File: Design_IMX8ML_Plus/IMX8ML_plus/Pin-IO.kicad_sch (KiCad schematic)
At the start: 3 parts, among them J1 DF40C-100DP-0.4V_51_, J2 DF40C-100DP-0.4V_51_, J3 DF40C-100DP-0.4V_51_

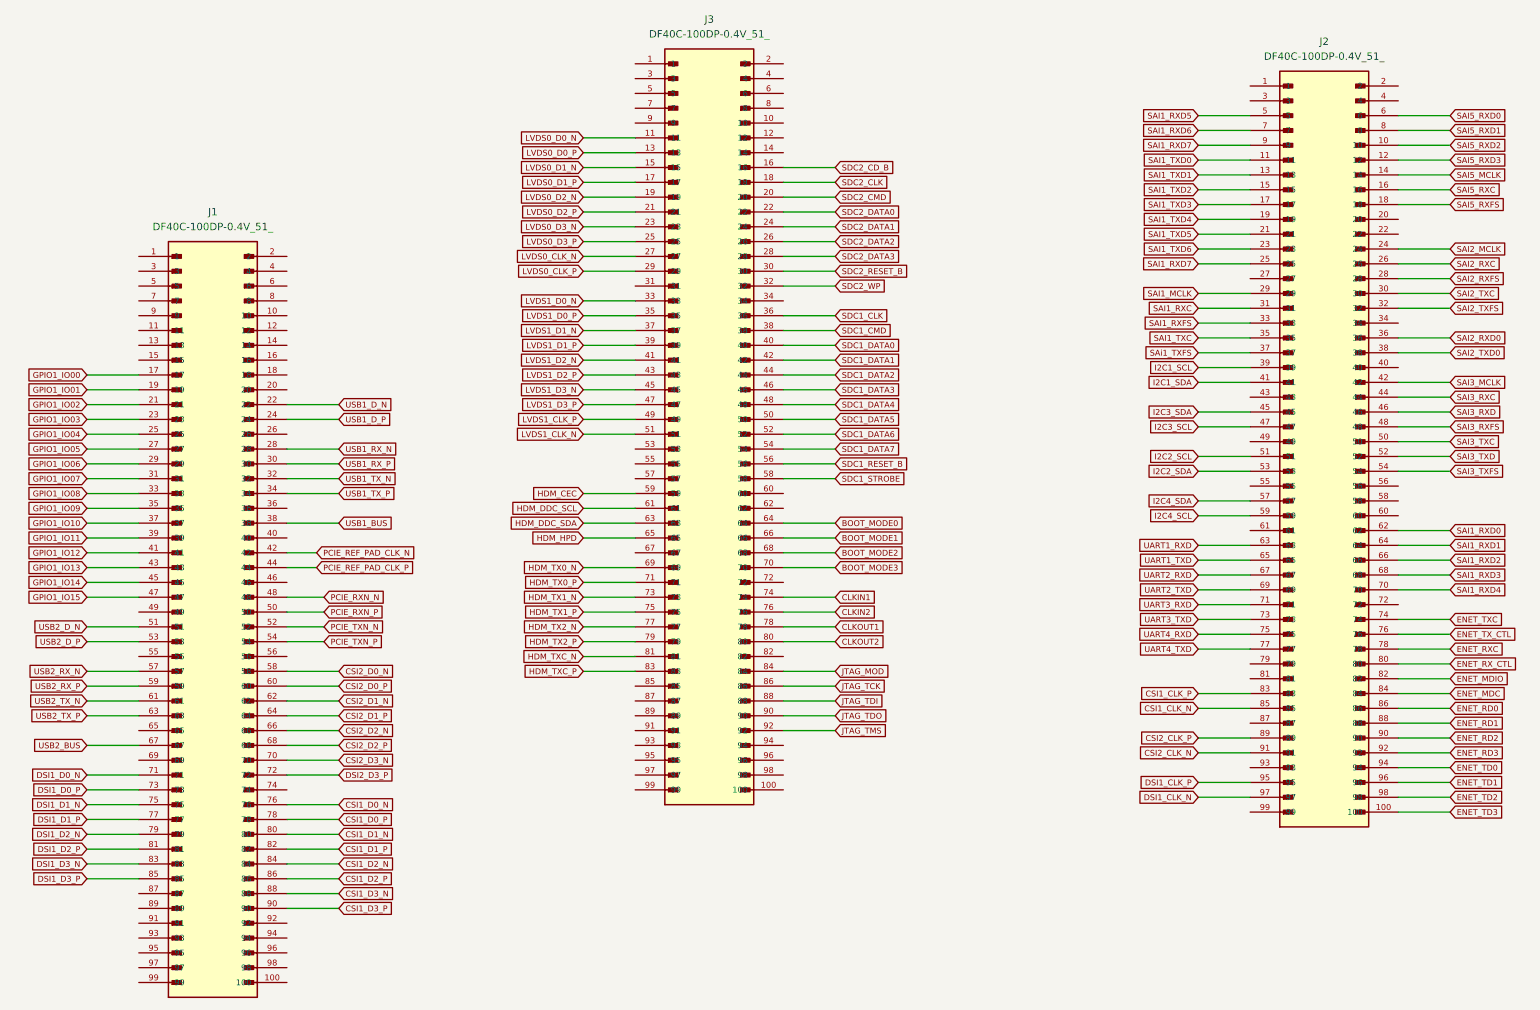
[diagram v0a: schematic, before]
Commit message: Update schematic and add ethernet interface ksz9131rn
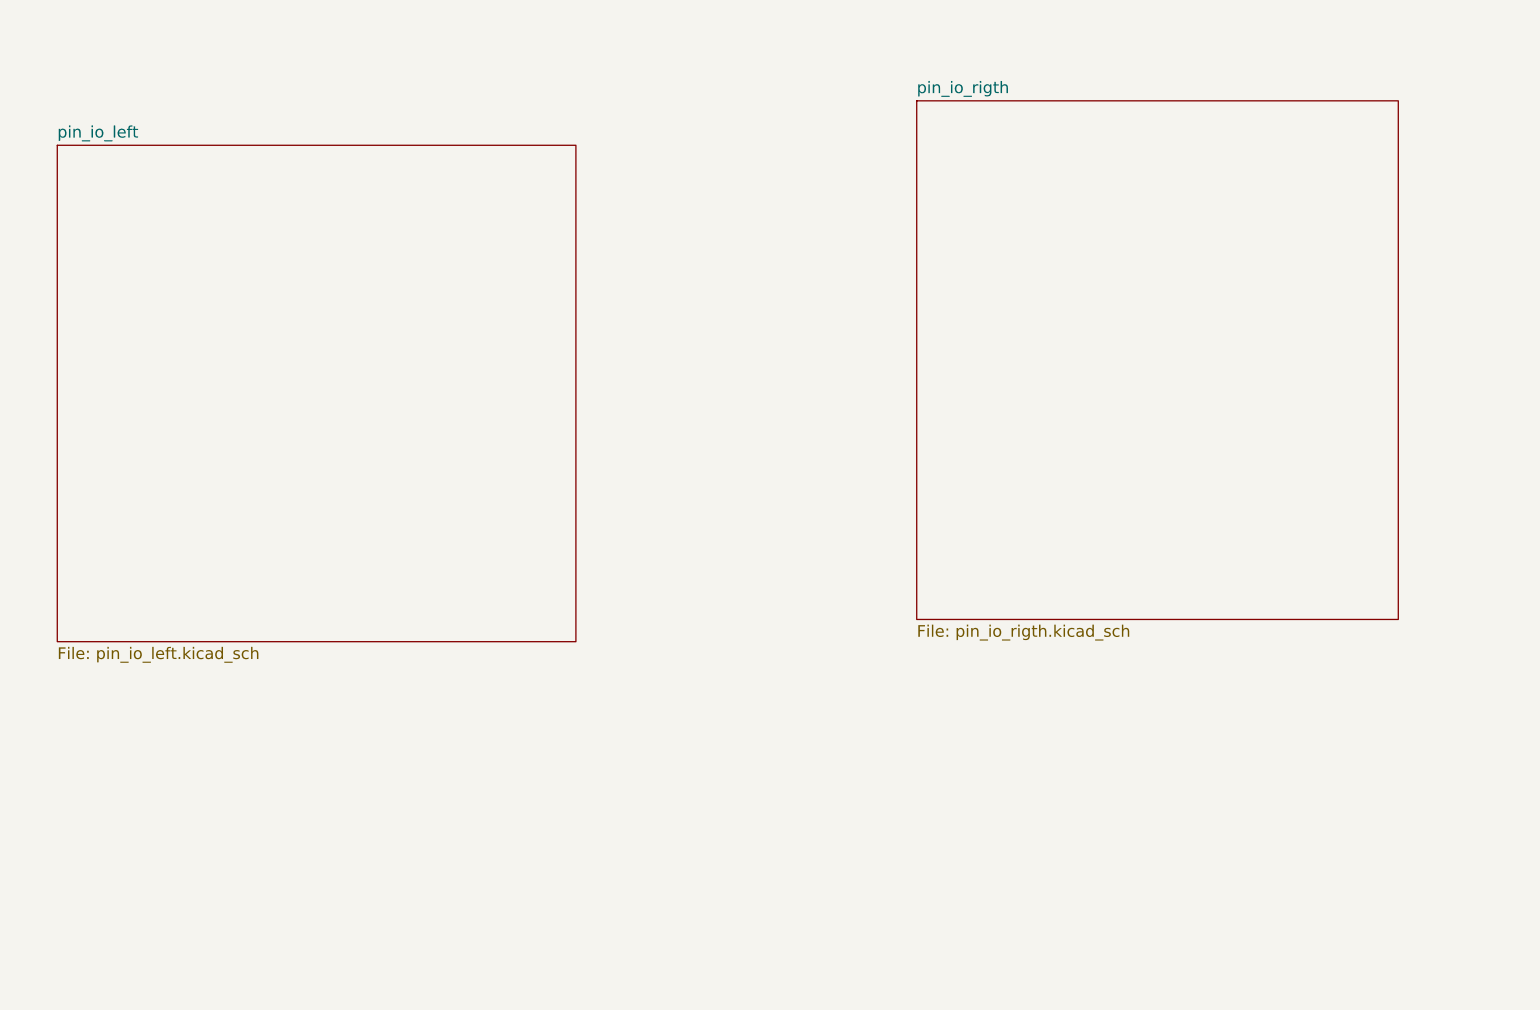
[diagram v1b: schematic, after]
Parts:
- removed J1, J2, J3: DF40C-100DP-0.4V_51_, _W_SBC:HIROSE_DF40C-100DS-0.4V_51_, symbol CONN_DF40C-100DS-0_4V51_HIR:DF40C-100DP-0.4V_51_
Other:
- added sheet pin_io_left (pin_io_left.kicad_sch)
- added sheet pin_io_rigth (pin_io_rigth.kicad_sch)

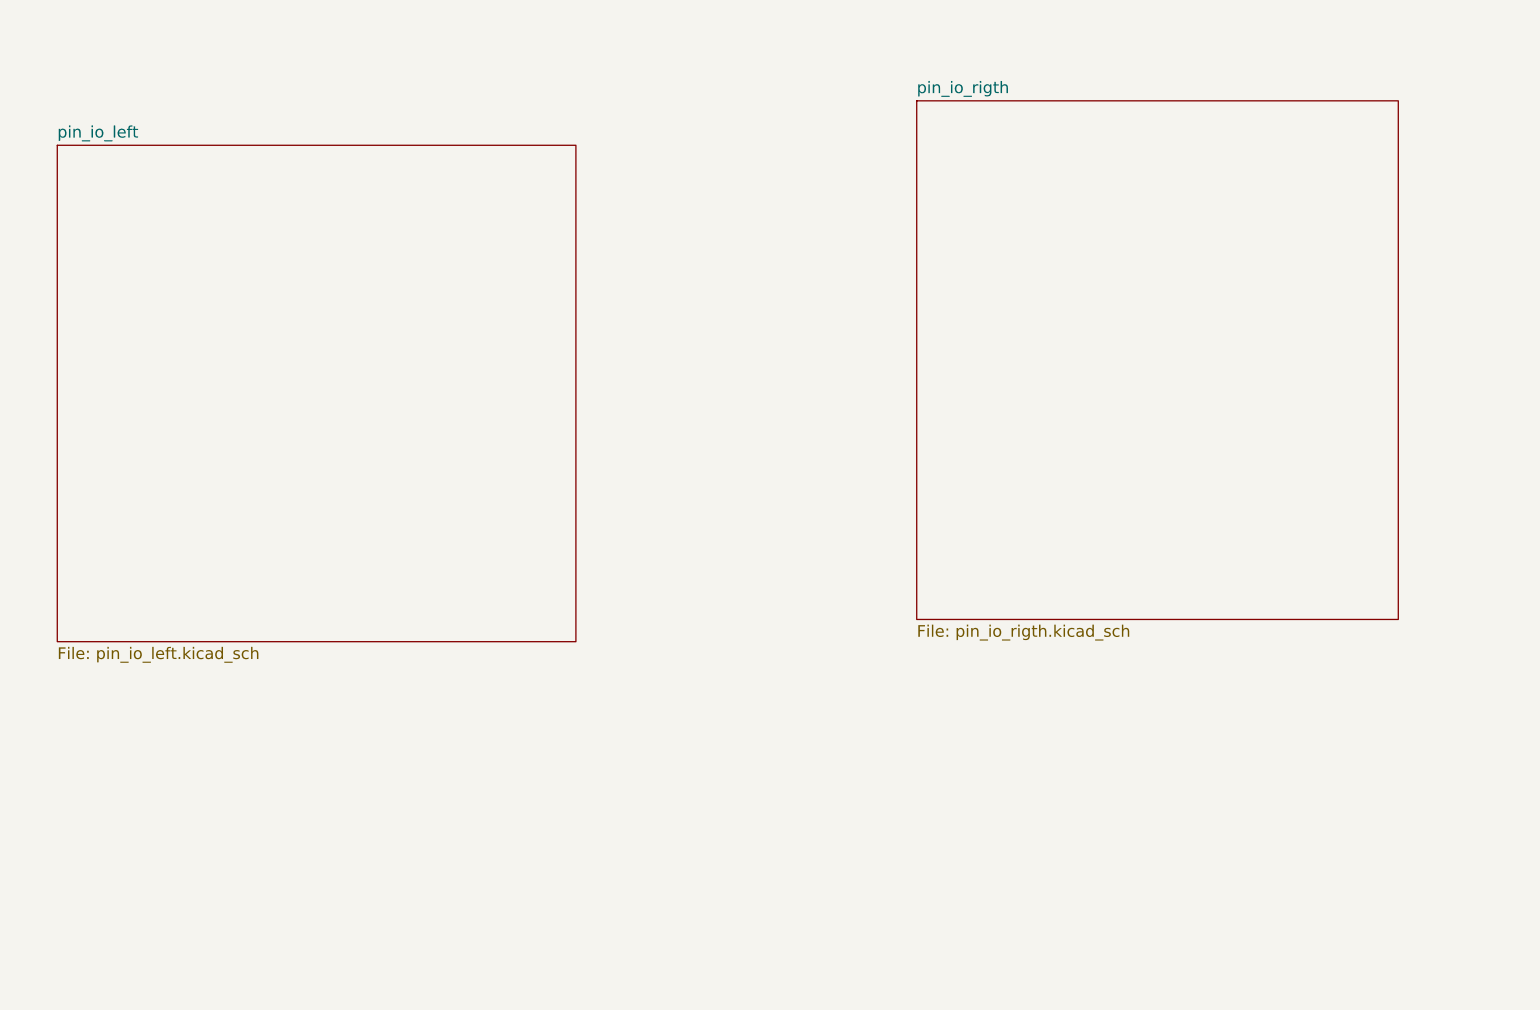
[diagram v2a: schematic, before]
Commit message: [IMX8ML-Processor] Reorganization of the pinout conector since processor to conectors
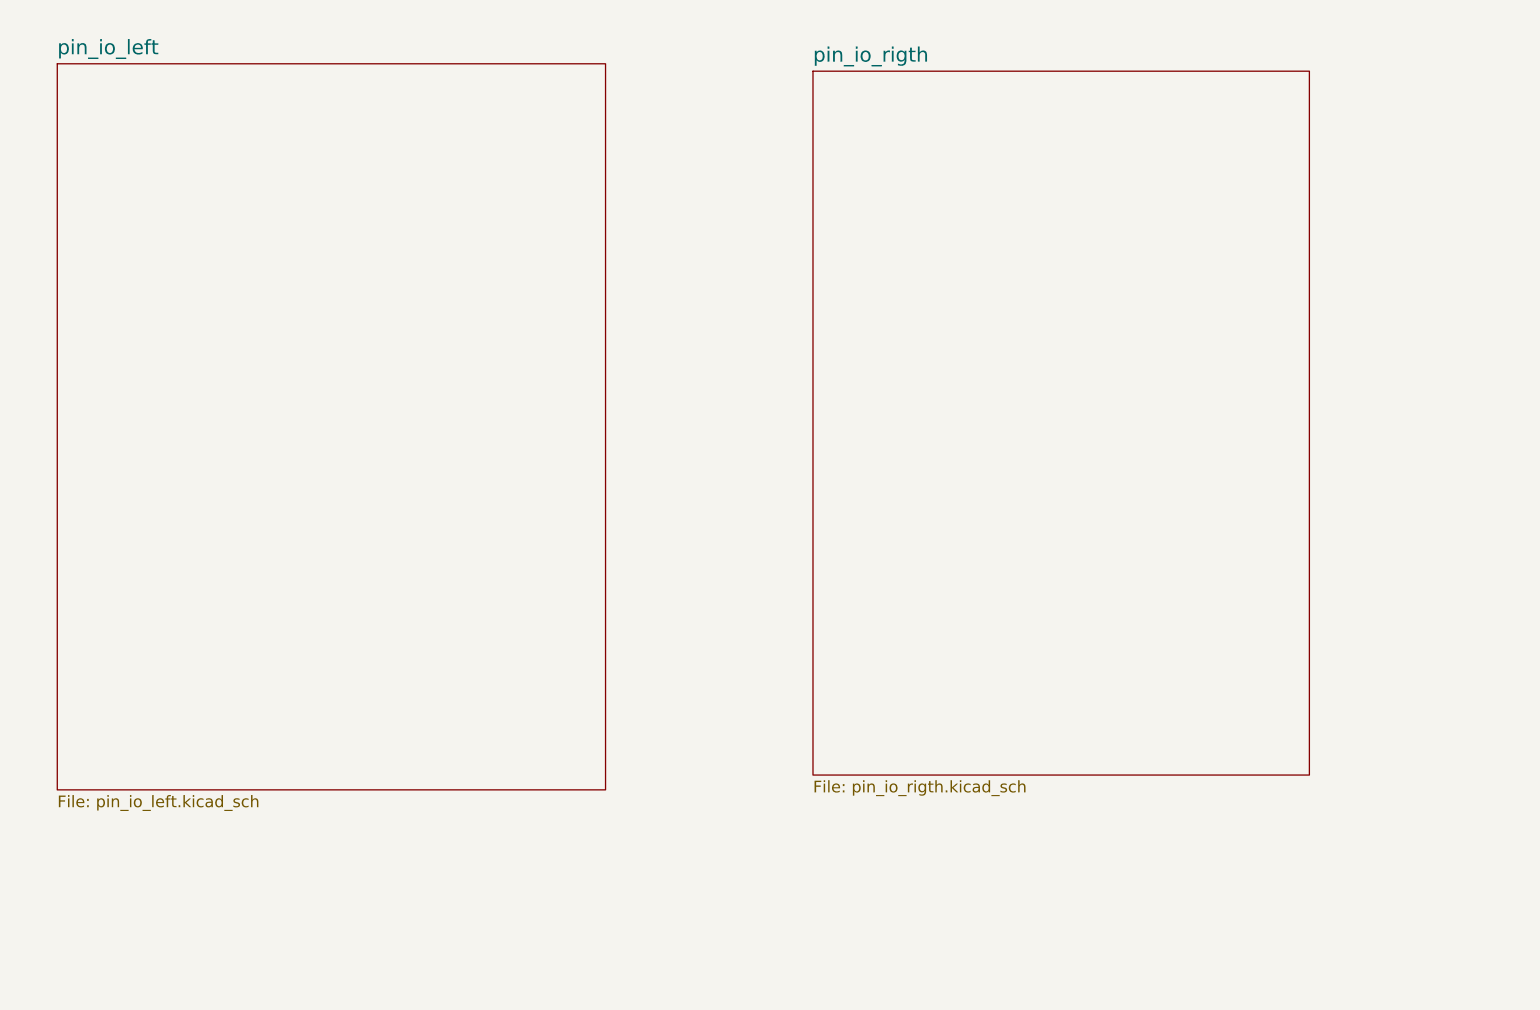
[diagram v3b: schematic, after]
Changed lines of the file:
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@@
 	(paper "A4")
 	(sheet
-		(at 171.45 31.75)
-		(size 82.55 88.9)
+		(at 153.67 26.67)
+		(size 85.09 120.65)
 		(fields_autoplaced yes)
 		(stroke
@@
 		)
 		(property "Sheetname" "pin_io_rigth"
-			(at 171.45 30.6734 0)
+			(at 153.67 25.3434 0)
 			(effects
 				(font
-					(size 2 2)
+					(size 2.5 2.5)
 				)
 				(justify left bottom)
@@
 		)
 		(property "Sheetfile" "pin_io_rigth.kicad_sch"
-			(at 171.45 121.5266 0)
+			(at 153.67 148.1966 0)
 			(effects
 				(font
@@
 	)
 	(sheet
-		(at 24.13 39.37)
-		(size 88.9 85.09)
+		(at 24.13 25.4)
+		(size 93.98 124.46)
 		(fields_autoplaced yes)
 		(stroke
@@
 		)
 		(property "Sheetname" "pin_io_left"
-			(at 24.13 38.2934 0)
+			(at 24.13 24.0734 0)
 			(effects
 				(font
-					(size 2 2)
+					(size 2.5 2.5)
 				)
 				(justify left bottom)
@@
 		)
 		(property "Sheetfile" "pin_io_left.kicad_sch"
-			(at 24.13 125.3366 0)
+			(at 24.13 150.7366 0)
 			(effects
 				(font
